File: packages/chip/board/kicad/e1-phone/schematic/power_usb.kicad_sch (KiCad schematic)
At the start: 0 parts

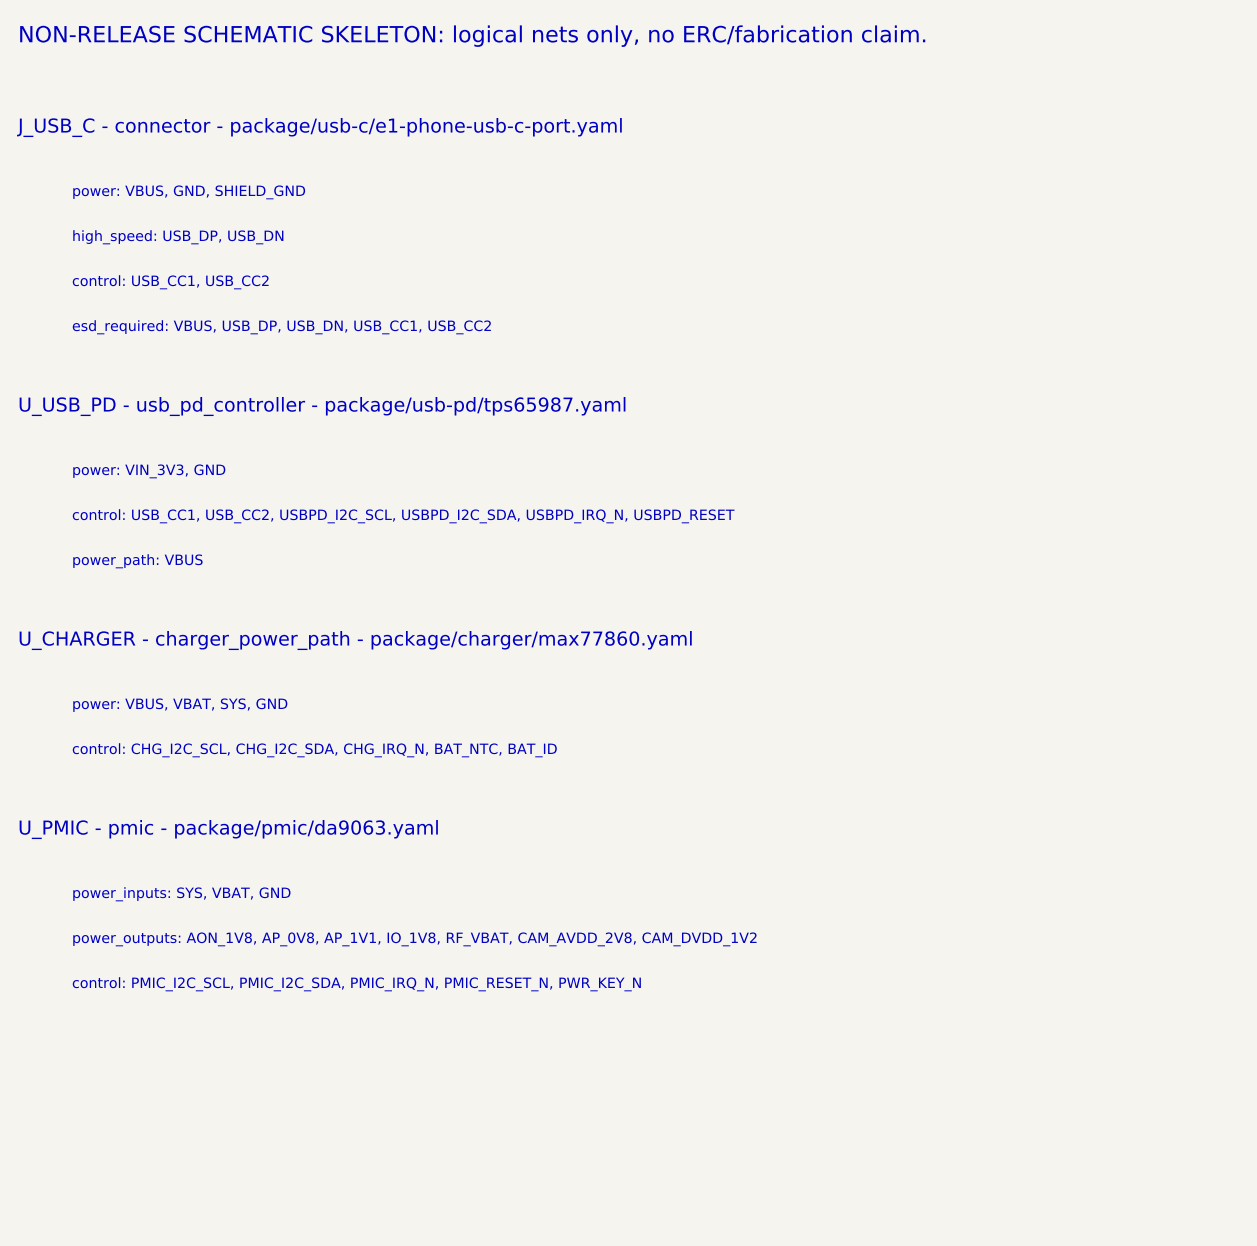
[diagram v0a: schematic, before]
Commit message: Prepare chip package for publishing
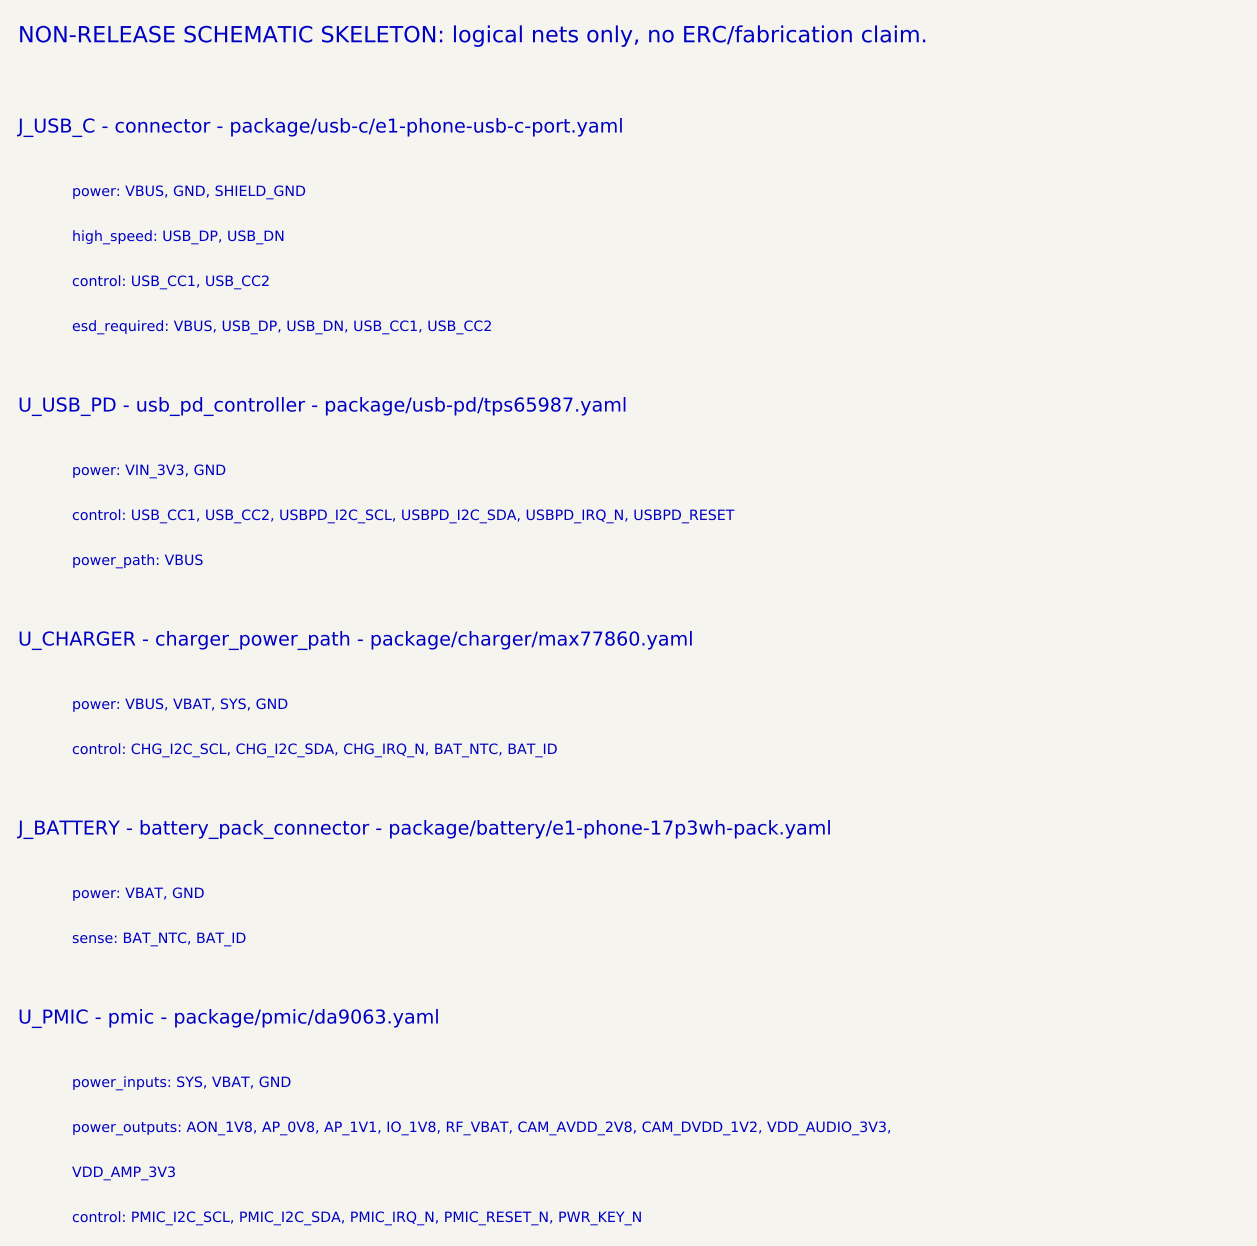
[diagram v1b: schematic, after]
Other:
- note added: "J_BATTERY - battery_pack_connector - package/battery/e1-phone-17p3wh-pack.yaml"
- note added: "VDD_AMP_3V3"
- note added: "power: VBAT, GND"
- note added: "power_outputs: AON_1V8, AP_0V8, AP_1V1, IO_1V8, RF_VBAT, CAM_AVDD_2V8, CAM_DVDD_1V2, VDD_AUDIO_3V3,"
- note added: "sense: BAT_NTC, BAT_ID"
- note removed: "power_outputs: AON_1V8, AP_0V8, AP_1V1, IO_1V8, RF_VBAT, CAM_AVDD_2V8, CAM_DVDD_1V2"
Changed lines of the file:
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@@
     (effects (font (size 1.15 1.15)) (justify left bottom))
   )
-  (text "U_PMIC - pmic - package/pmic/da9063.yaml" (at 20.00 108.00 0)
+  (text "J_BATTERY - battery_pack_connector - package/battery/e1-phone-17p3wh-pack.yaml" (at 20.00 108.00 0)
     (effects (font (size 1.55 1.55)) (justify left bottom))
   )
-  (text "power_inputs: SYS, VBAT, GND" (at 26.00 115.00 0)
+  (text "power: VBAT, GND" (at 26.00 115.00 0)
     (effects (font (size 1.15 1.15)) (justify left bottom))
   )
-  (text "power_outputs: AON_1V8, AP_0V8, AP_1V1, IO_1V8, RF_VBAT, CAM_AVDD_2V8, CAM_DVDD_1V2" (at 26.00 120.00 0)
+  (text "sense: BAT_NTC, BAT_ID" (at 26.00 120.00 0)
     (effects (font (size 1.15 1.15)) (justify left bottom))
   )
-  (text "control: PMIC_I2C_SCL, PMIC_I2C_SDA, PMIC_IRQ_N, PMIC_RESET_N, PWR_KEY_N" (at 26.00 125.00 0)
+  (text "U_PMIC - pmic - package/pmic/da9063.yaml" (at 20.00 129.00 0)
+    (effects (font (size 1.55 1.55)) (justify left bottom))
+  )
+  (text "power_inputs: SYS, VBAT, GND" (at 26.00 136.00 0)
     (effects (font (size 1.15 1.15)) (justify left bottom))
   )
+  (text "power_outputs: AON_1V8, AP_0V8, AP_1V1, IO_1V8, RF_VBAT, CAM_AVDD_2V8, CAM_DVDD_1V2, VDD_AUDIO_3V3," (at 26.00 141.00 0)
+    (effects (font (size 1.15 1.15)) (justify left bottom))
+  )
+  (text "VDD_AMP_3V3" (at 26.00 146.00 0)
+    (effects (font (size 1.15 1.15)) (justify left bottom))
+  )
+  (text "control: PMIC_I2C_SCL, PMIC_I2C_SDA, PMIC_IRQ_N, PMIC_RESET_N, PWR_KEY_N" (at 26.00 151.00 0)
+    (effects (font (size 1.15 1.15)) (justify left bottom))
+  )
